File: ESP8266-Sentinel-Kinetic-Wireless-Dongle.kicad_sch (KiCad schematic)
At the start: 61 parts, among them J1 Conn_01x04, J2 Screw_Terminal_01x04, J3 Conn_01x06_Pin, J4 RJ9, J5 Screw_Terminal_01x03, J6 Screw_Terminal_01x04, Q1 SS8050, Q2 AO3401A, Q3 AO3400A, SW2 SW_Push, SW4 SW_Push, U1 AMS1117-3.3, U2 ESP-12E, U3 MAX3232, U4 ESP32-WROOM-32, U5 L78L10_SOT89, U6 74AHCT125

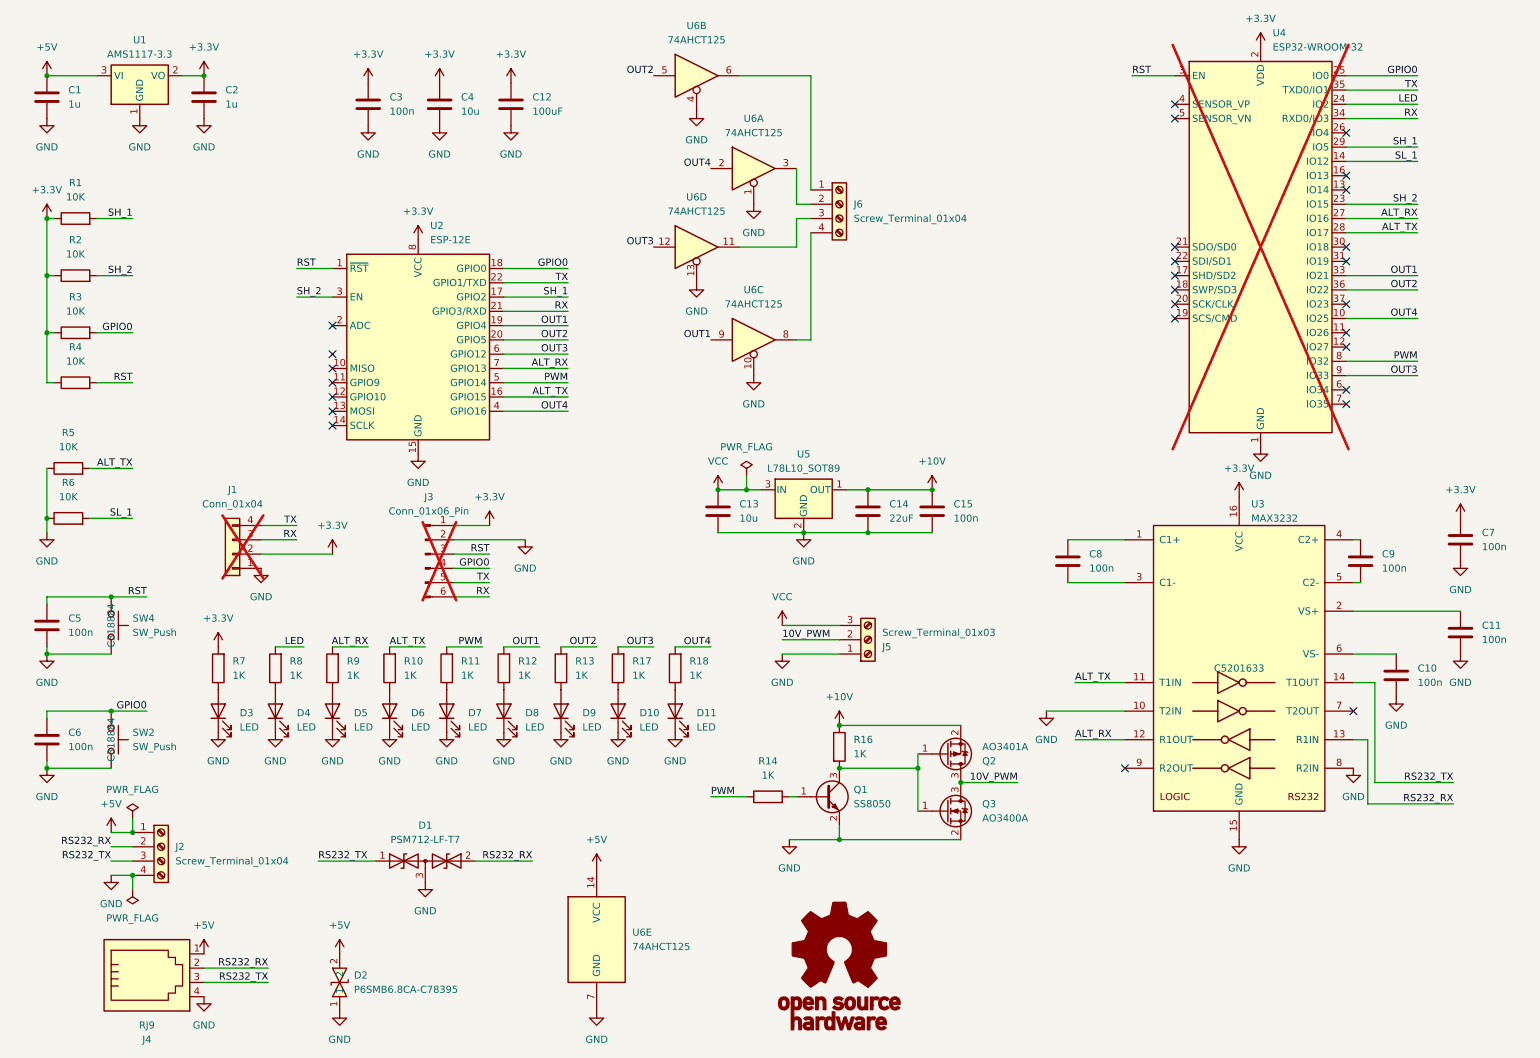
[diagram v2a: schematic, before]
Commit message: corrected rx and tx positions for lilygo downloader
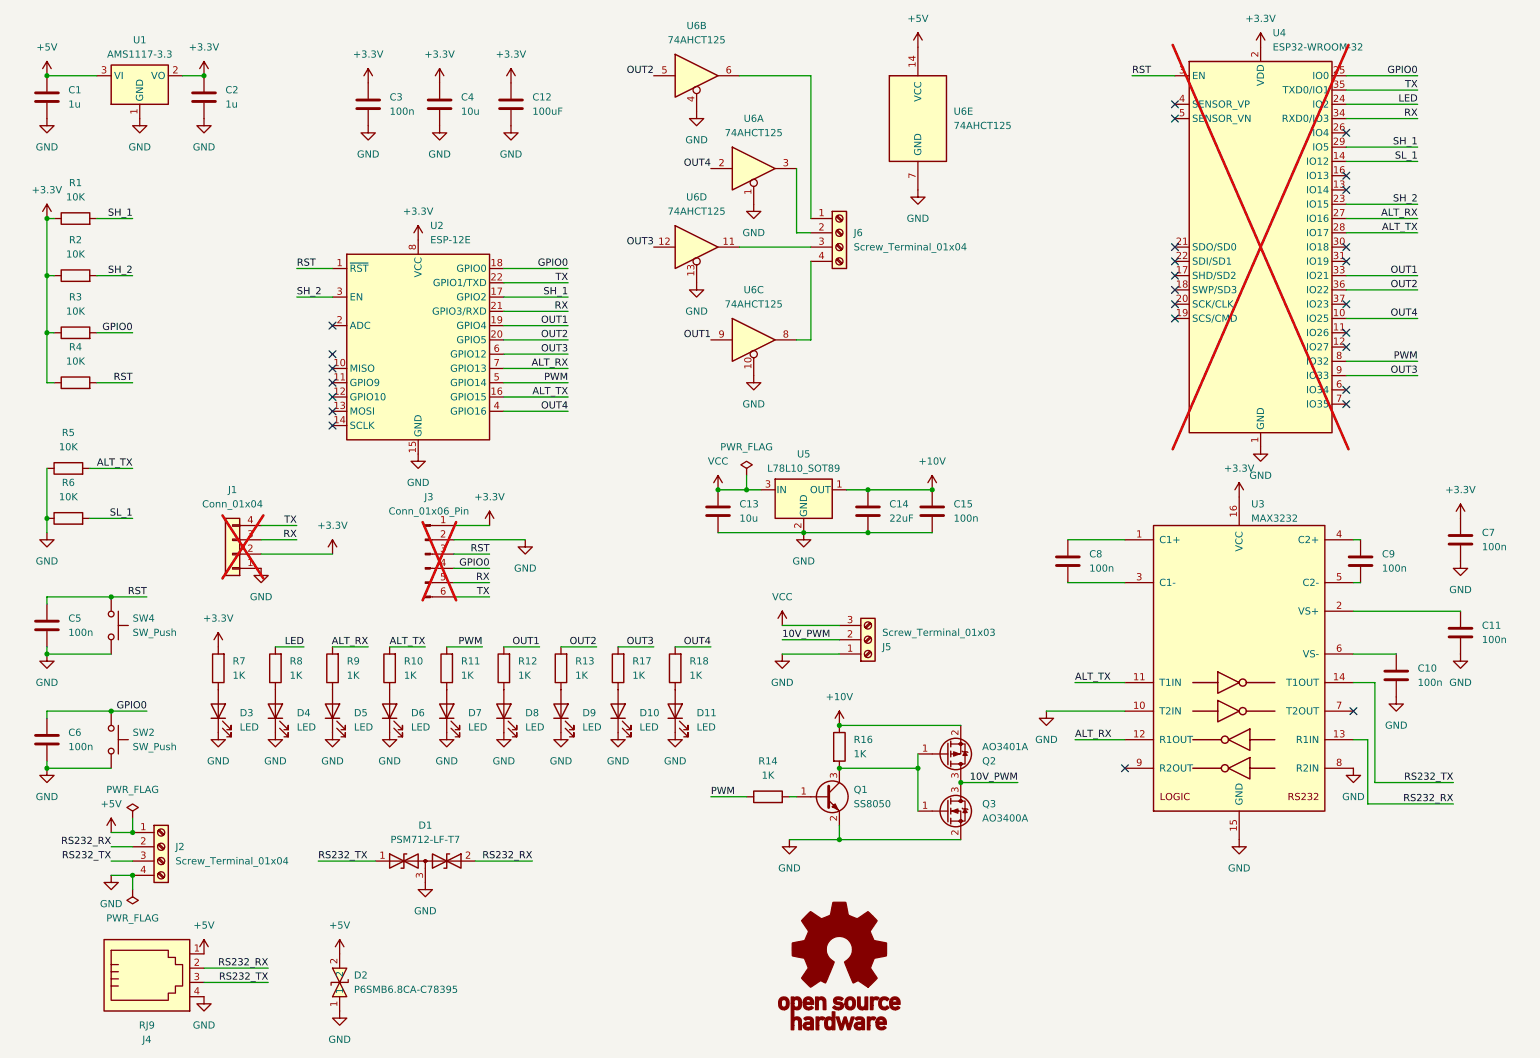
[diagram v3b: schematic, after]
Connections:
- net RX: now also J3.5 (Pin_5); no longer J3.6 (Pin_6)
- net TX: now also J3.6 (Pin_6); no longer J3.5 (Pin_5)
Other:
- moved on the sheet: J6, U6E
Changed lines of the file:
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@@
 	(wire
 		(pts
-			(xy 156.21 52.07) (xy 156.21 71.12)
+			(xy 156.21 57.15) (xy 156.21 71.12)
 		)
 		(stroke
@@
 	(wire
 		(pts
+			(xy 92.71 116.84) (xy 99.06 116.84)
+		)
+		(stroke
+			(width 0)
+			(type default)
+		)
+	)
+	(wire
+		(pts
 			(xy 101.6 63.5) (xy 113.03 63.5)
 		)
@@
 	(wire
 		(pts
-			(xy 153.67 46.99) (xy 153.67 40.64)
+			(xy 153.67 52.07) (xy 153.67 40.64)
 		)
 		(stroke
@@
 	(wire
 		(pts
-			(xy 153.67 54.61) (xy 153.67 49.53)
-		)
-		(stroke
-			(width 0)
-			(type default)
-		)
-	)
-	(wire
-		(pts
 			(xy 101.6 81.28) (xy 113.03 81.28)
 		)
@@
 	(wire
 		(pts
-			(xy 156.21 44.45) (xy 156.21 24.13)
+			(xy 156.21 49.53) (xy 156.21 24.13)
 		)
 		(stroke
@@
 	(wire
 		(pts
-			(xy 92.71 116.84) (xy 99.06 116.84)
-		)
-		(stroke
-			(width 0)
-			(type default)
-		)
-	)
-	(wire
-		(pts
-			(xy 153.67 49.53) (xy 156.21 49.53)
-		)
-		(stroke
-			(width 0)
-			(type default)
-		)
-	)
-	(wire
-		(pts
 			(xy 144.78 97.79) (xy 147.32 97.79)
 		)
@@
 	(wire
 		(pts
-			(xy 156.21 46.99) (xy 153.67 46.99)
+			(xy 156.21 52.07) (xy 153.67 52.07)
 		)
 		(stroke
@@
 	(wire
 		(pts
+			(xy 92.71 114.3) (xy 99.06 114.3)
+		)
+		(stroke
+			(width 0)
+			(type default)
+		)
+	)
+	(wire
+		(pts
 			(xy 256.54 149.86) (xy 256.54 132.08)
 		)
@@
 	(wire
 		(pts
-			(xy 153.67 54.61) (xy 143.51 54.61)
+			(xy 143.51 54.61) (xy 156.21 54.61)
 		)
 		(stroke
@@
 	(wire
 		(pts
-			(xy 92.71 114.3) (xy 99.06 114.3)
-		)
-		(stroke
-			(width 0)
-			(type default)
-		)
-	)
-	(wire
-		(pts
 			(xy 107.95 125.73) (xy 101.6 125.73)
 		)
@@
 	)
 	(label "TX"
-		(at 99.06 114.3 180)
+		(at 99.06 116.84 180)
 		(effects
 			(font
@@
 	)
 	(label "RX"
-		(at 99.06 116.84 180)
+		(at 99.06 114.3 180)
 		(effects
 			(font
@@
 					(size 1.27 1.27)
 				)
+				(hide yes)
 			)
 		)
@@
 	(symbol
 		(lib_id "power:+5V")
-		(at 118.11 165.1 0)
+		(at 175.26 19.05 0)
 		(unit 1)
 		(exclude_from_sim no)
@@
 		(fields_autoplaced yes)
 		(property "Reference" "#PWR037"
-			(at 118.11 168.91 0)
+			(at 175.26 22.86 0)
 			(effects
 				(font
@@
 		)
 		(property "Value" "+5V"
-			(at 118.11 160.02 0)
+			(at 175.26 13.97 0)
 			(effects
 				(font
@@
 		)
 		(property "Footprint" ""
-			(at 118.11 165.1 0)
+			(at 175.26 19.05 0)
 			(effects
 				(font
@@
 		)
 		(property "Datasheet" ""
-			(at 118.11 165.1 0)
+			(at 175.26 19.05 0)
 			(effects
 				(font
@@
 		)
 		(property "Description" "Power symbol creates a global label with name \"+5V\""
-			(at 118.11 165.1 0)
+			(at 175.26 19.05 0)
 			(effects
 				(font
@@
 	(symbol
 		(lib_id "power:GND")
-		(at 118.11 190.5 0)
+		(at 175.26 44.45 0)
 		(unit 1)
 		(exclude_from_sim no)
@@
 		(fields_autoplaced yes)
 		(property "Reference" "#PWR055"
-			(at 118.11 196.85 0)
+			(at 175.26 50.8 0)
 			(effects
 				(font
@@
 		)
 		(property "Value" "GND"
-			(at 118.11 195.58 0)
+			(at 175.26 49.53 0)
 			(effects
 				(font
@@
 		)
 		(property "Footprint" ""
-			(at 118.11 190.5 0)
+			(at 175.26 44.45 0)
 			(effects
 				(font
@@
 		)
 		(property "Datasheet" ""
-			(at 118.11 190.5 0)
+			(at 175.26 44.45 0)
 			(effects
 				(font
@@
 		)
 		(property "Description" "Power symbol creates a global label with name \"GND\" , ground"
-			(at 118.11 190.5 0)
+			(at 175.26 44.45 0)
 			(effects
 				(font
@@
 	(symbol
 		(lib_id "74xx:74AHCT125")
-		(at 118.11 177.8 0)
+		(at 175.26 31.75 0)
 		(unit 5)
 		(exclude_from_sim no)
@@
 		(fields_autoplaced yes)
 		(property "Reference" "U6"
-			(at 124.46 176.5299 0)
+			(at 181.61 30.4799 0)
 			(effects
 				(font
@@
 		)
 		(property "Value" "74AHCT125"
-			(at 124.46 179.0699 0)
+			(at 181.61 33.0199 0)
 			(effects
 				(font
@@
 		)
 		(property "Footprint" "Package_DIP:DIP-14_W7.62mm"
-			(at 118.11 177.8 0)
+			(at 175.26 31.75 0)
 			(effects
 				(font
@@
 		)
 		(property "Datasheet" "https://www.ti.com/lit/ds/symlink/sn74ahct125.pdf"
-			(at 118.11 177.8 0)
+			(at 175.26 31.75 0)
 			(effects
 				(font
@@
 		)
 		(property "Description" "Quadruple Bus Buffer Gates With 3-State Outputs"
-			(at 118.11 177.8 0)
+			(at 175.26 31.75 0)
 			(effects
 				(font
@@
 	(symbol
 		(lib_id "Connector:Screw_Terminal_01x04")
-		(at 161.29 46.99 0)
+		(at 161.29 52.07 0)
 		(unit 1)
 		(exclude_from_sim no)
@@
 		(dnp no)
 		(property "Reference" "J6"
-			(at 163.83 46.9899 0)
+			(at 163.83 52.0699 0)
 			(effects
 				(font
@@
 		)
 		(property "Value" "Screw_Terminal_01x04"
-			(at 163.83 49.5299 0)
+			(at 163.83 54.6099 0)
 			(effects
 				(font
@@
 		)
 		(property "Footprint" "TerminalBlock_4Ucon:TerminalBlock_4Ucon_1x04_P3.50mm_Horizontal"
-			(at 161.29 46.99 0)
+			(at 161.29 52.07 0)
 			(effects
 				(font
@@
 		)
 		(property "Datasheet" "~"
-			(at 161.29 46.99 0)
+			(at 161.29 52.07 0)
 			(effects
 				(font
@@
 		)
 		(property "Description" "Generic screw terminal, single row, 01x04, script generated (kicad-library-utils/schlib/autogen/connector/)"
-			(at 161.29 46.99 0)
+			(at 161.29 52.07 0)
 			(effects
 				(font
@@
 		)
 		(property "LCSC" ""
-			(at 161.29 46.99 0)
+			(at 161.29 52.07 0)
 			(effects
 				(font
@@
 					(size 1.27 1.27)
 				)
+				(hide yes)
 			)
 		)
@@
 					(size 1.27 1.27)
 				)
+				(hide yes)
 			)
 		)

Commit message: Include push buttons in BOM
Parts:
- SW2, SW4: now in the parts list
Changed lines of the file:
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@@
 		(unit 1)
 		(exclude_from_sim no)
-		(in_bom no)
+		(in_bom yes)
 		(on_board yes)
 		(dnp no)
@@
 		(unit 1)
 		(exclude_from_sim no)
-		(in_bom no)
+		(in_bom yes)
 		(on_board yes)
 		(dnp no)

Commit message: Added Silkscreen markings to Diagnostic LED's Inverted Serial LED's, so LED is only on when signal is sent or recieved.
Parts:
- U2: now not fitted; now left out of the parts list
- U4: now fitted
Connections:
- net +3.3V: now also D5.2 (A), D6.2 (A)
- net ALT_RX: now also R9.1; no longer R9.2
- net ALT_TX: now also R10.1; no longer R10.2
- net GND: no longer D5.1 (K), D6.1 (K)
- new net: D6.1 (K), R10.2
- new net: D5.1 (K), R9.2
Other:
- moved on the sheet: D5, D6, R10, R9
